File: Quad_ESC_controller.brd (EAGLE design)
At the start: 25.8 x 34.2 mm, 24 parts, among them Y1 ECS-80-S-4X

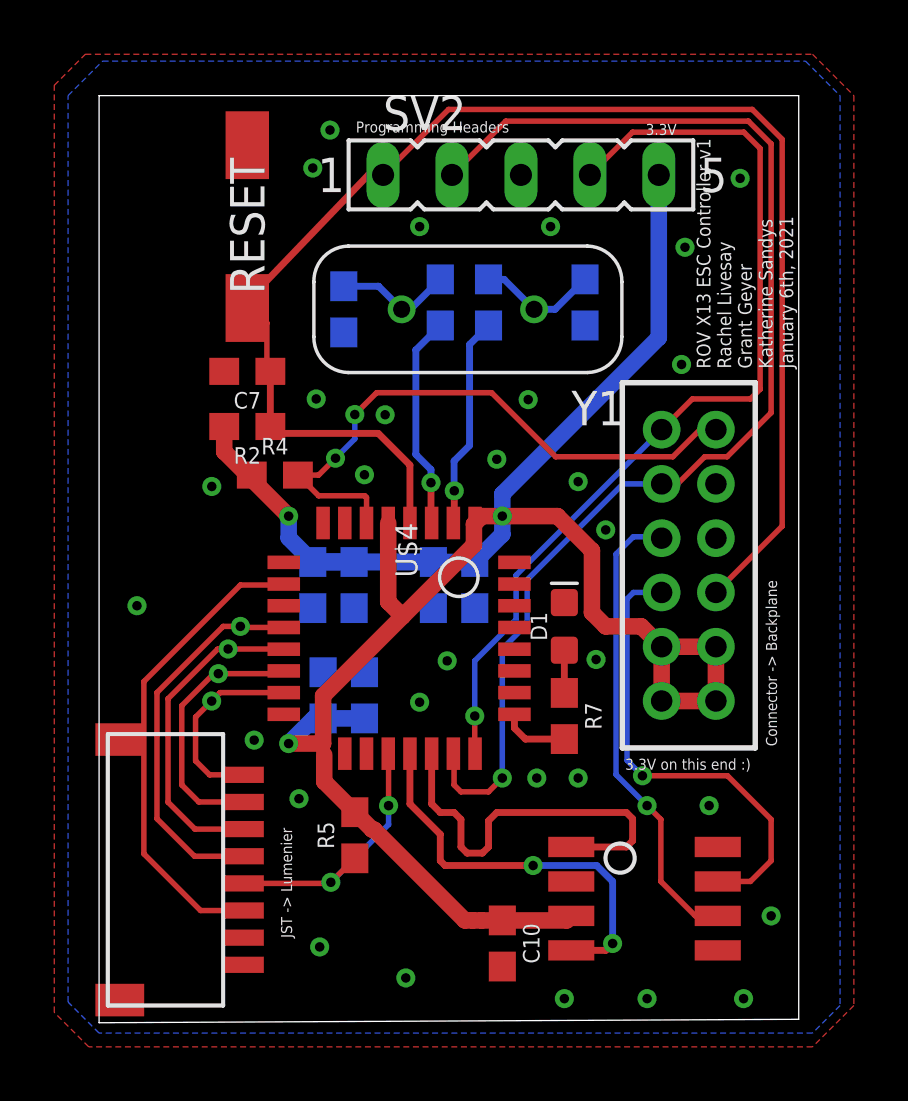
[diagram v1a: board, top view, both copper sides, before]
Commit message: Add op amp for telemetry logic level fixing
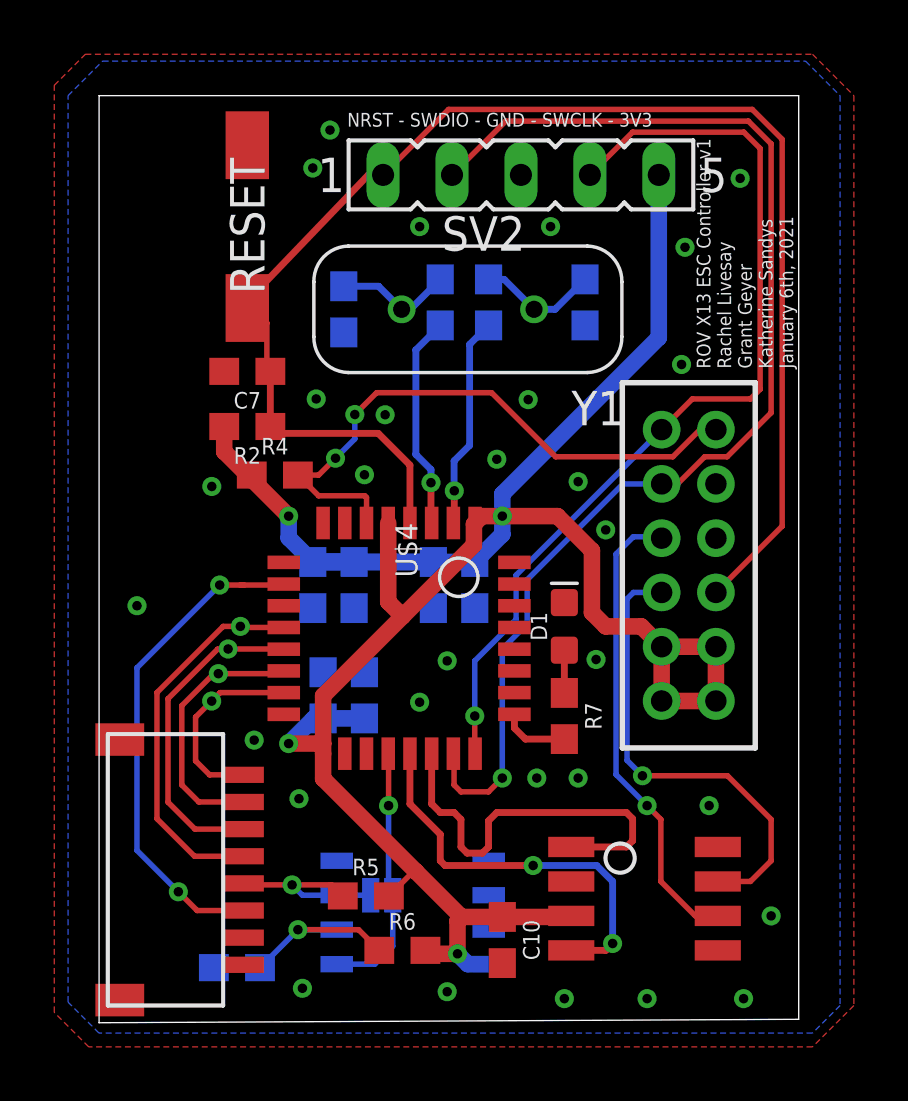
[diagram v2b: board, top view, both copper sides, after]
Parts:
- added IC1: OP-AMP, SparkFun-IC-Amplifiers:SO08
- added JP1: JUMPER-SMT_2_NO_SILK, SparkFun-Jumpers:SMT-JUMPER_2_NO_SILK
- added R6: 1k, SparkFun-Resistors:0603
- added R8: 3.3k, SparkFun-Resistors:0603
- moved R5 2.27 mm to (9.83, 4.67), turned to 0 degrees
- moved C10 0.13 mm to (14.9, 3.05)
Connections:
- new net N$6: IC1.2, R6.1, R8.2
- new net TLM_ESC: IC1.3, JP1.1, R5.1, U$2.4
- net +3V3: now also IC1.8, R6.2
- net GND: now also IC1.4, R8.1
- net TLM: now also IC1.1, JP1.2; no longer R5.1, U$2.4
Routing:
- net TLM_ESC: track 0.00 -> 6.90 mm, vias 0 -> 1
- net N$6: track 0.00 -> 6.72 mm, vias 0 -> 1
- net +3V3: track 84.7 -> 90.3 mm, vias 3 -> 4
- net ADC: track 17.5 -> 18.3 mm, vias 0 -> 2
- net TLM: track 10.2 -> 9.50 mm, vias 2 -> 1
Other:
- board text added: "NRST - SWDIO - GND - SWCLK - 3V3"
- board text removed: "3.3V"
- board text removed: "3.3V on this end :)"
- board text removed: "Connector -> Backplane"
- board text removed: "JST -> Lumenier"
- board text removed: "Programming Headers"

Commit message: New SWD programming connector
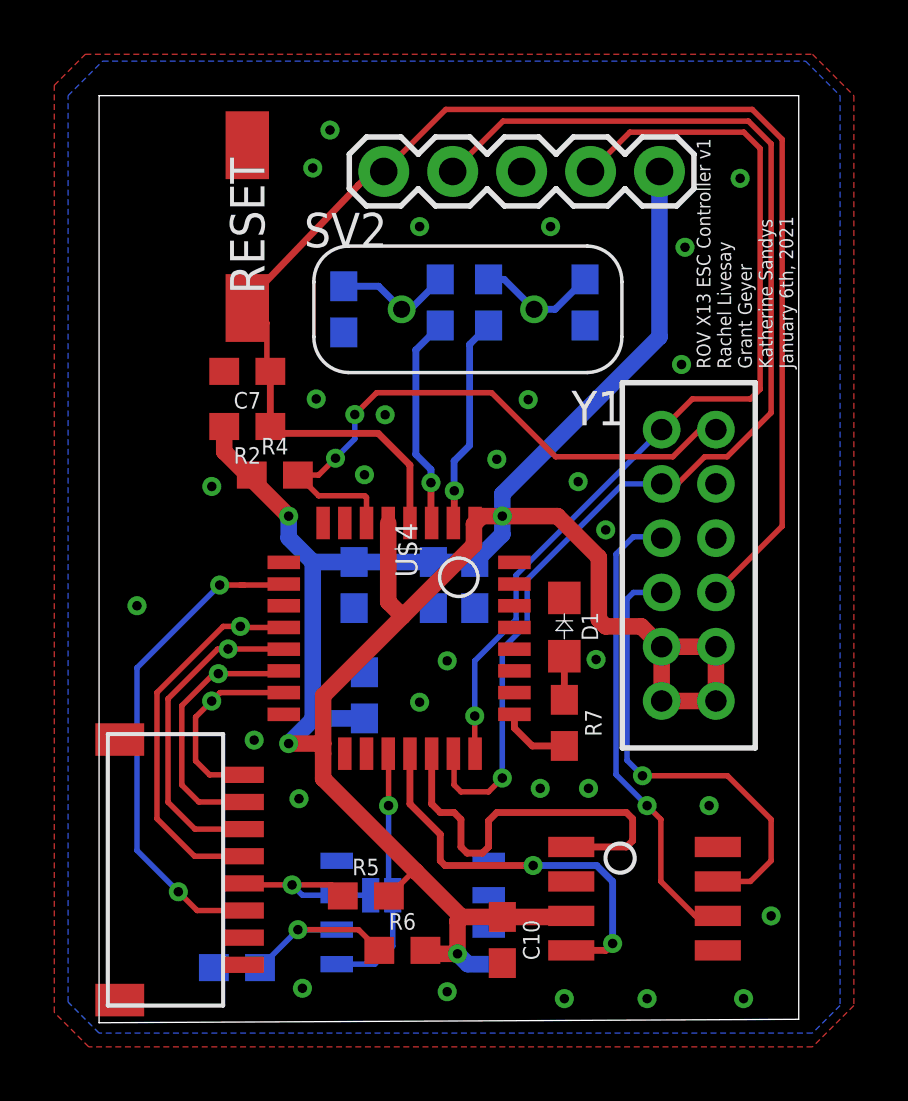
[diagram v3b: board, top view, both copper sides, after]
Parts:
- removed C4, C6: 4.7uF, SparkFun-Capacitors:0603
- C2, C3, C5: value 4.7uF -> 0.1uF
- D1: value (none) -> COLOR; device SparkFun-LED:LED-0603 -> LED, 0805:0805
- SV2: value (none) -> 3V3 -SWCLK-GND-SWDIO- NRST; device con-lsta:FE05-1 -> CONN, Serial Wire Programming Headers:1X05
- moved SV2 5.11 mm to (20.7, 31.4), turned to 180 degrees
- moved R7 0.25 mm to (17.1, 11.0)
- turned D1 to 270 degrees
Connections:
- net +3V3: now also SV2.1; no longer C4.1, C6.1, SV2.5
- net GND: no longer C4.2, C6.2
- net NRST: now also SV2.5; no longer SV2.1
- net SWCLK: now also SV2.2; no longer SV2.4
- net SWDIO: now also SV2.4; no longer SV2.2
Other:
- board text removed: "NRST - SWDIO - GND - SWCLK - 3V3"

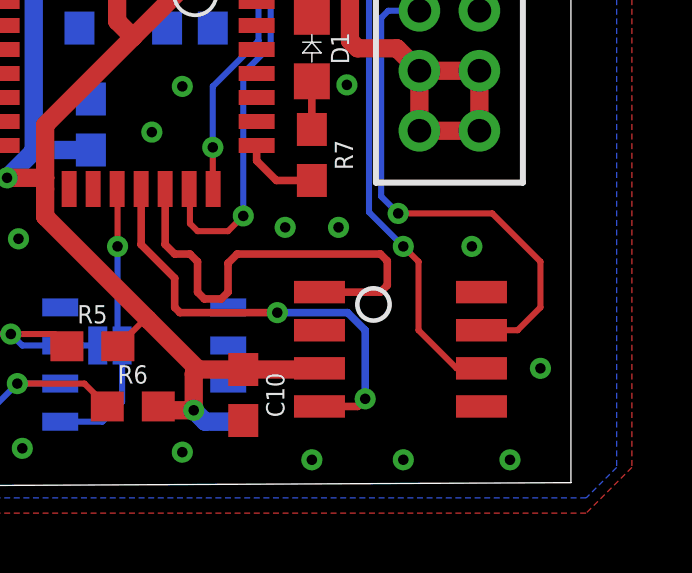
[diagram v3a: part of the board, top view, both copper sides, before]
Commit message: Use aluminum caps for the adapter board
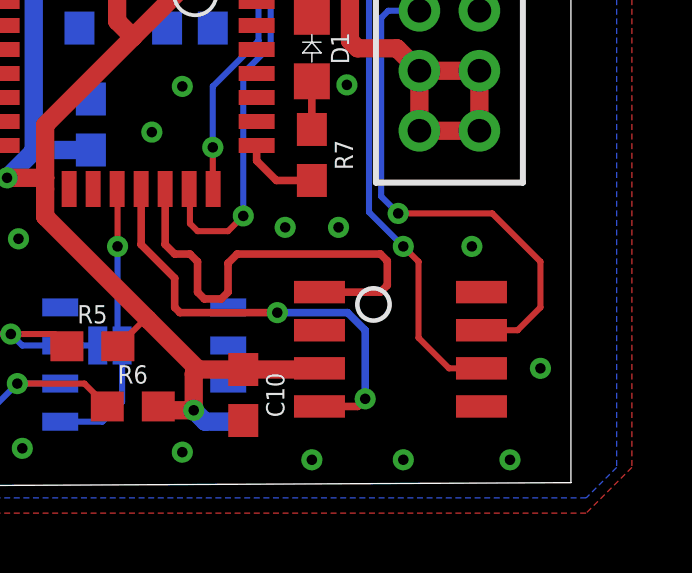
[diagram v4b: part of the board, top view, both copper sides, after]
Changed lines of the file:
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@@
 <via x="20.193" y="8.001" extent="1-16" drill="0.35"/>
 <wire x1="20.193" y1="8.001" x2="20.701" y2="7.493" width="0.2032" layer="1"/>
-<wire x1="20.701" y1="7.493" x2="20.701" y2="5.207" width="0.2032" layer="1"/>
-<wire x1="20.701" y1="5.207" x2="21.971" y2="3.937" width="0.2032" layer="1"/>
-<wire x1="21.971" y1="3.937" x2="22.799" y2="3.937" width="0.2032" layer="1"/>
+<wire x1="20.701" y1="7.493" x2="20.701" y2="4.953" width="0.2032" layer="1"/>
+<wire x1="20.701" y1="4.953" x2="21.717" y2="3.937" width="0.2032" layer="1"/>
+<wire x1="21.717" y1="3.937" x2="22.799" y2="3.937" width="0.2032" layer="1"/>
 <wire x1="19.05" y1="9.144" x2="20.193" y2="8.001" width="0.2032" layer="16"/>
 </signal>
